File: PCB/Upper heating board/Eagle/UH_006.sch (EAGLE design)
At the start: 5 parts, among them X3 MKDSN1,5/4-5,08

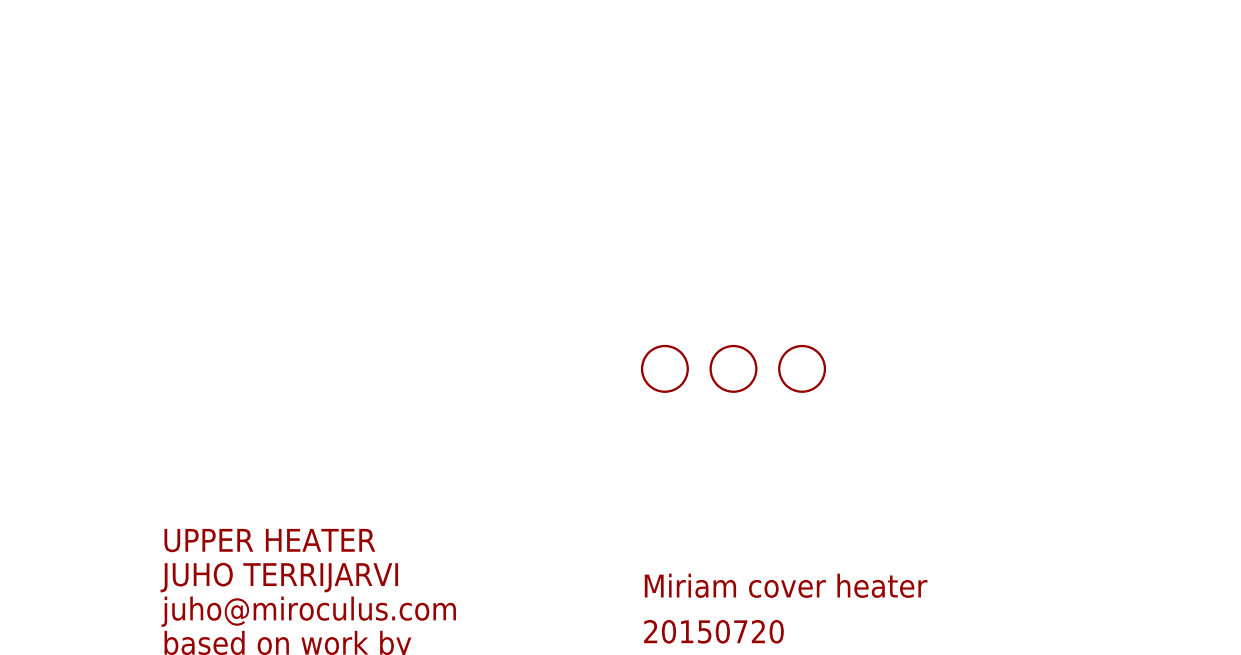
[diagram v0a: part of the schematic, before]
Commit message: PCB modification, CERN license
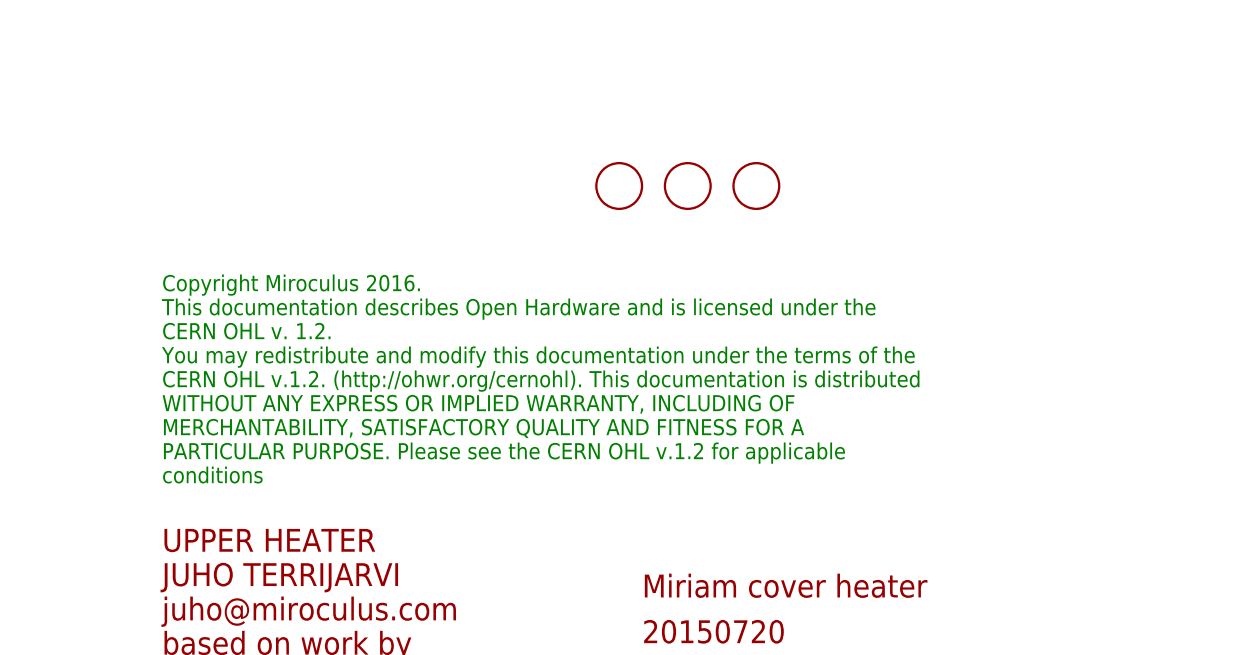
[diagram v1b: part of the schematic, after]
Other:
- note added: "Copyright Miroculus 2016. This documentation describes Open Hardware and is licensed under the CERN OHL v. 1.2. You may redistribute and modify this documentation under the terms of the CERN OHL v.1.2. (http://ohwr.org/cernohl). This documentation is distributed WITHOUT ANY EXPRESS OR IMPLIED WARRANTY, INCLUDING OF MERCHANTABILITY, SATISFACTORY QUALITY AND FITNESS FOR A PARTICULAR PURPOSE. Please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"
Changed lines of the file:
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@@
 <text x="218.44" y="20.32" size="2.54" layer="94" font="vector" rot="MR180">Miriam cover heater</text>
 <text x="218.44" y="15.24" size="2.54" layer="94" font="vector" rot="MR180">20150720</text>
+<text x="165.1" y="30.48" size="1.778" layer="91">Copyright Miroculus 2016.
+This documentation describes Open Hardware and is licensed under the
+CERN OHL v. 1.2.
+You may redistribute and modify this documentation under the terms of the
+CERN OHL v.1.2. (http://ohwr.org/cernohl). This documentation is distributed
+WITHOUT ANY EXPRESS OR IMPLIED WARRANTY, INCLUDING OF
+MERCHANTABILITY, SATISFACTORY QUALITY AND FITNESS FOR A
+PARTICULAR PURPOSE. Please see the CERN OHL v.1.2 for applicable
+conditions</text>
 </plain>
 <instances>
@@
 <attribute name="VALUE" x="53.34" y="139.7" size="1.778" layer="96"/>
 </instance>
-<instance part="FD1" gate="G$1" x="220.98" y="43.18"/>
+<instance part="FD1" gate="G$1" x="215.9" y="63.5"/>
 <instance part="FRAME2" gate="G$1" x="2.54" y="2.54" smashed="yes">
 <attribute name="SHEET" x="233.045" y="7.62" size="2.54" layer="94"/>
@@
 </instance>
 <instance part="TH1" gate="G$1" x="27.94" y="96.52"/>
-<instance part="FD2" gate="G$1" x="228.6" y="43.18"/>
-<instance part="FD3" gate="G$1" x="236.22" y="43.18"/>
+<instance part="FD2" gate="G$1" x="223.52" y="63.5"/>
+<instance part="FD3" gate="G$1" x="231.14" y="63.5"/>
 </instances>
 <busses>
